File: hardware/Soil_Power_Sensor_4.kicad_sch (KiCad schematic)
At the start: 10 parts, among them J5 BOOT, J6 UART, U9 ESP32-C3-MINI-1-N4

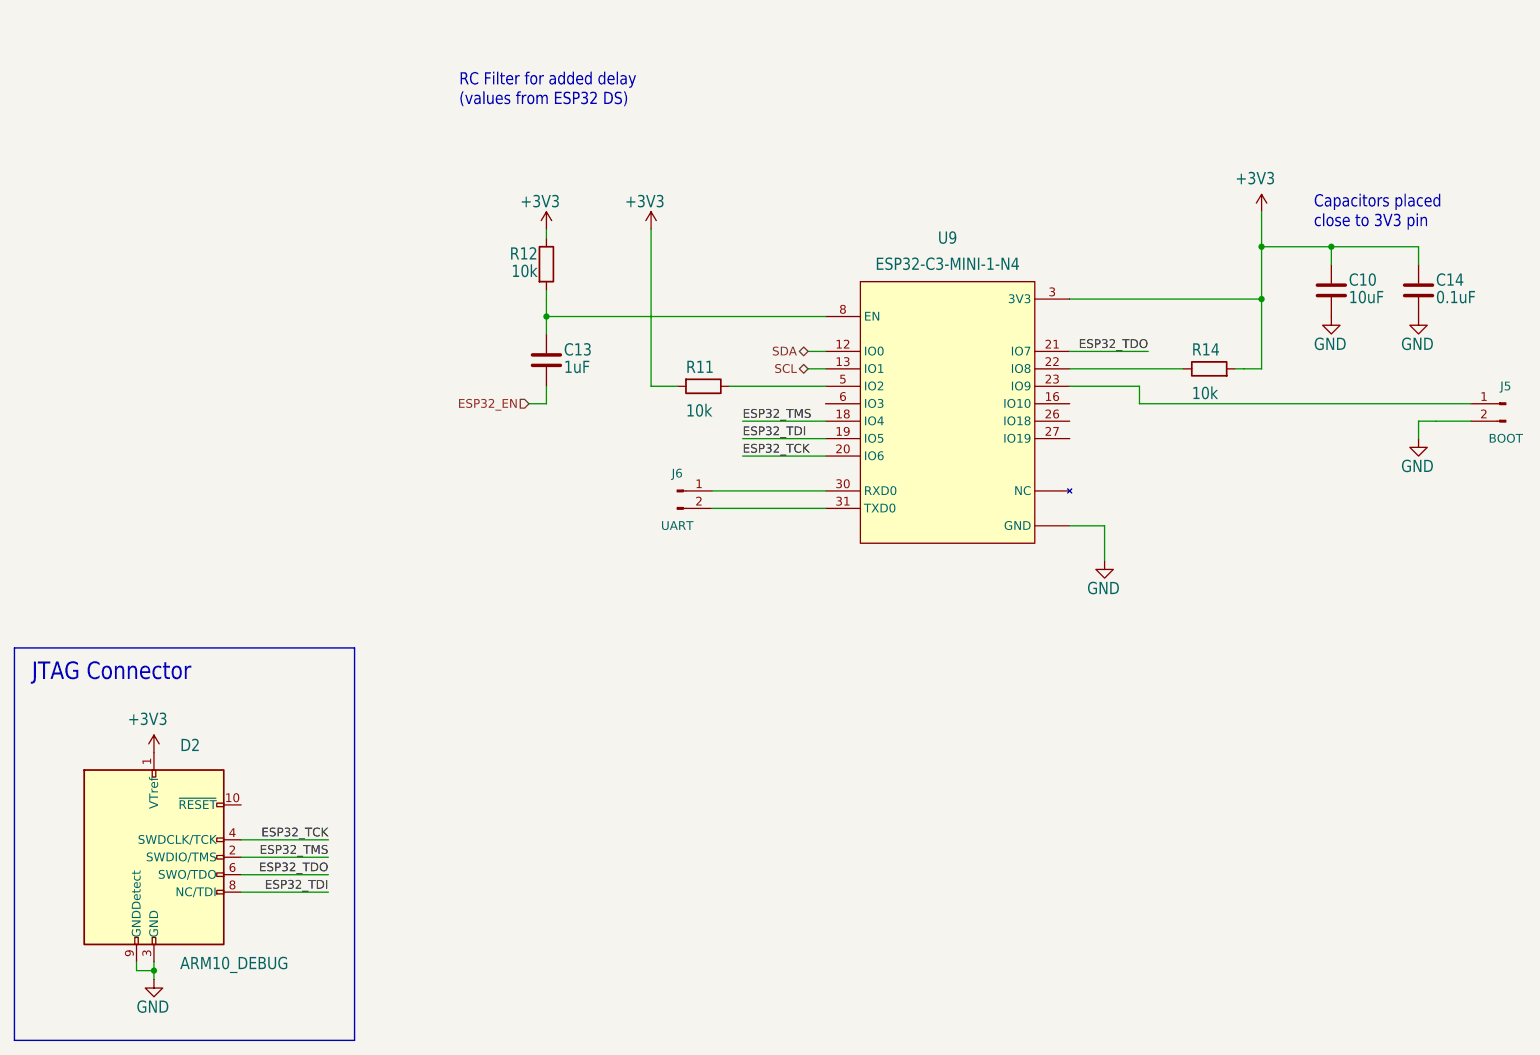
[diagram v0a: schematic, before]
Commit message: Adding general improvements to sensor PCB
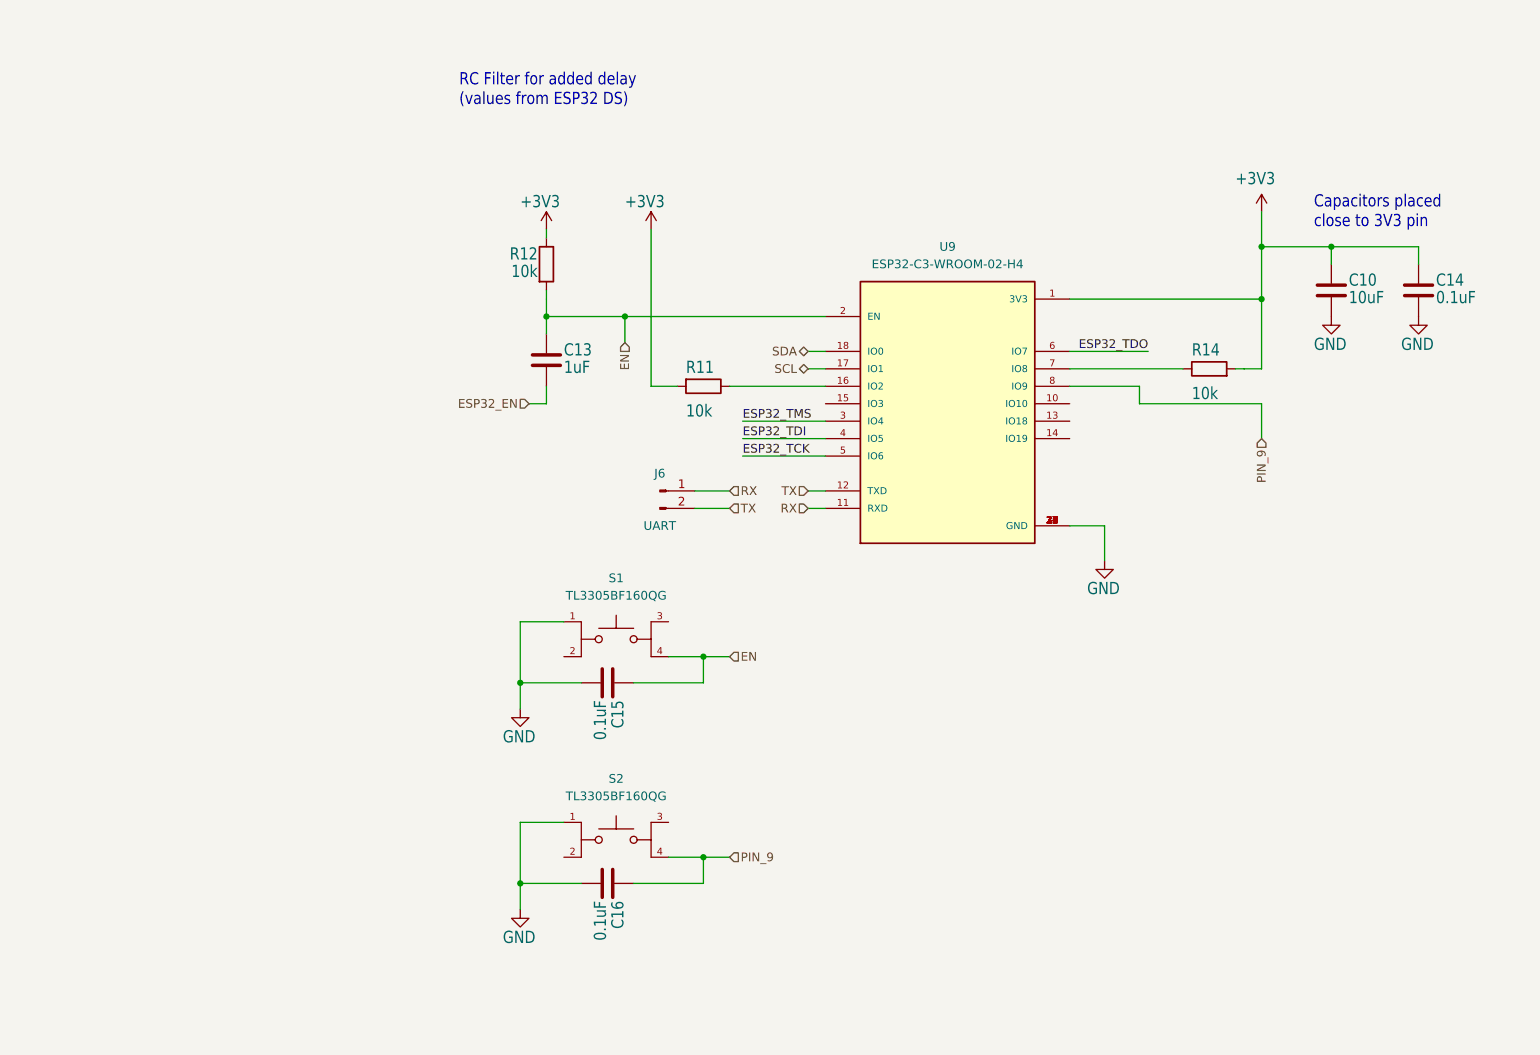
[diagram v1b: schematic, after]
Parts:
- removed D2: ARM10_DEBUG, Soil Power Sensor:ARM10_DEBUG, symbol Connector:Conn_ARM_JTAG_SWD_10
- removed J5: BOOT, Connector_PinHeader_2.54mm:PinHeader_1x02_P2.54mm_Vertical, symbol Connector:Conn_01x02_Pin
- removed U9: ESP32-C3-MINI-1-N4, Soil Power Sensor:XCVR_ESP32-C3-MINI-1-N4, symbol Soil Power Sensor-eagle-import:ESP32-C3-MINI-1-N4
- added C15, C16: 0.1uF, Capacitor_SMD:C_0603_1608Metric, symbol Device:C
- added S1, S2: TL3305BF160QG, TL3305BF160QG:SW_TL3305BF160QG, symbol TL3305BF160QG:TL3305BF160QG
- added U9: ESP32-C3-WROOM-02-H4, ESP32-C3-WROOM-02-H4:MODULE_ESP32-C3-WROOM-02-H4, symbol ESP32-C3-WROOM-02-H4:ESP32-C3-WROOM-02-H4
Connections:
- net +3V3: now also U9.1 (3V3)
- net ESP32_TCK: now also U9.5 (IO6)
- net ESP32_TDI: now also U9.4 (IO5)
- net ESP32_TDO: now also U9.6 (IO7)
- net ESP32_TMS: now also U9.3 (IO4)
- net GND: now also C15.2, C16.2, S1.1, S2.1, U9.19 (GND), U9.20 (GND), U9.21 (GND), U9.22 (GND), U9.23 (GND), U9.24 (GND), U9.25 (GND), U9.26 (GND), U9.27 (GND), U9.28 (GND), U9.29 (GND), U9.30 (GND), U9.31 (GND), U9.32 (GND), U9.33 (GND), U9.34 (GND), U9.35 (GND), U9.36 (GND), U9.37 (GND), U9.38 (GND), U9.39 (GND), U9.9 (GND)
- net SCL: now also U9.17 (IO1)
- net SDA: now also U9.18 (IO0)
- net at R11.1: now also U9.16 (IO2)
- net EN: now reaches C13.1, R12.2
- net EN: now also C15.1, S1.4, U9.2 (EN)
- net at R14.1: now also U9.7 (IO8)
- net RX: now reaches J6.1 (Pin_1)
- net RX: now also U9.11 (RXD)
- net TX: now reaches J6.2 (Pin_2)
- net TX: now also U9.12 (TXD)
- new net PIN_9: C16.1, S2.4, U9.8 (IO9)
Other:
- note removed: "JTAG Connector"
- moved on the sheet: J6

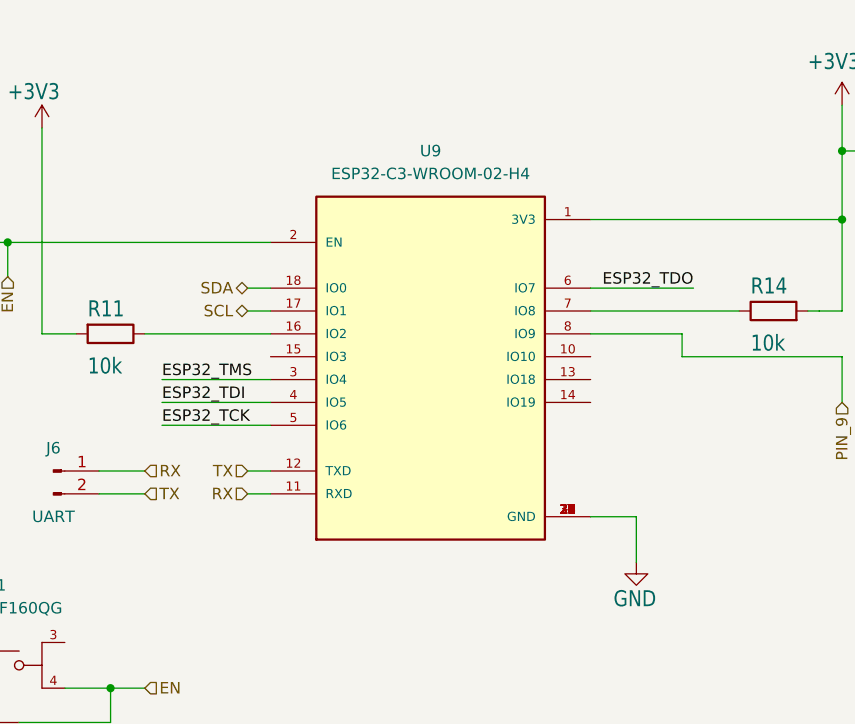
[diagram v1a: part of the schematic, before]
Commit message: Updated ESP32 module
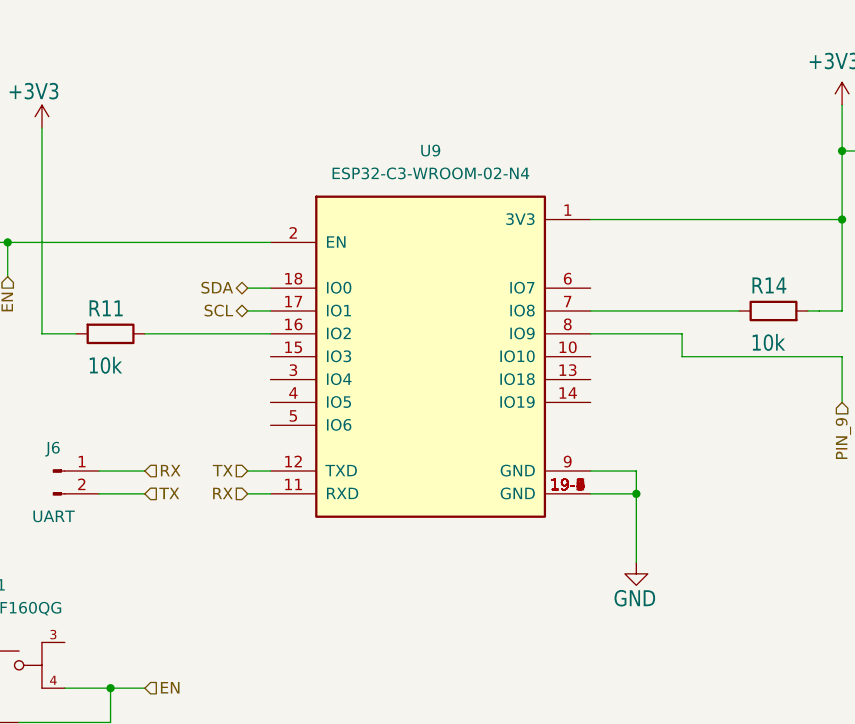
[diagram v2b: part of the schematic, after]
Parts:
- removed U9: ESP32-C3-WROOM-02-H4, ESP32-C3-WROOM-02-H4:MODULE_ESP32-C3-WROOM-02-H4, symbol ESP32-C3-WROOM-02-H4:ESP32-C3-WROOM-02-H4
- added U9: ESP32-C3-WROOM-02-N4, Soil Power Sensor:MODULE_ESP32-C3-WROOM-02-N4, symbol Soil Power Sensor-eagle-import:ESP32-C3-WROOM-02-N4
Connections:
- net +3V3: now also U9.1 (3V3)
- net EN: now also U9.2 (EN)
- net GND: now also U9.19-1 (GND), U9.19-2 (GND), U9.19-3 (GND), U9.19-4 (GND), U9.19-5 (GND), U9.19-6 (GND), U9.19-7 (GND), U9.19-8 (GND), U9.19-9 (GND), U9.9 (GND)
- net PIN_9: now also U9.8 (IO9)
- net RX: now also U9.11 (RXD)
- net SCL: now also U9.17 (IO1)
- net SDA: now also U9.18 (IO0)
- net TX: now also U9.12 (TXD)
- net at R11.1: now also U9.16 (IO2)
- net at R14.1: now also U9.7 (IO8)

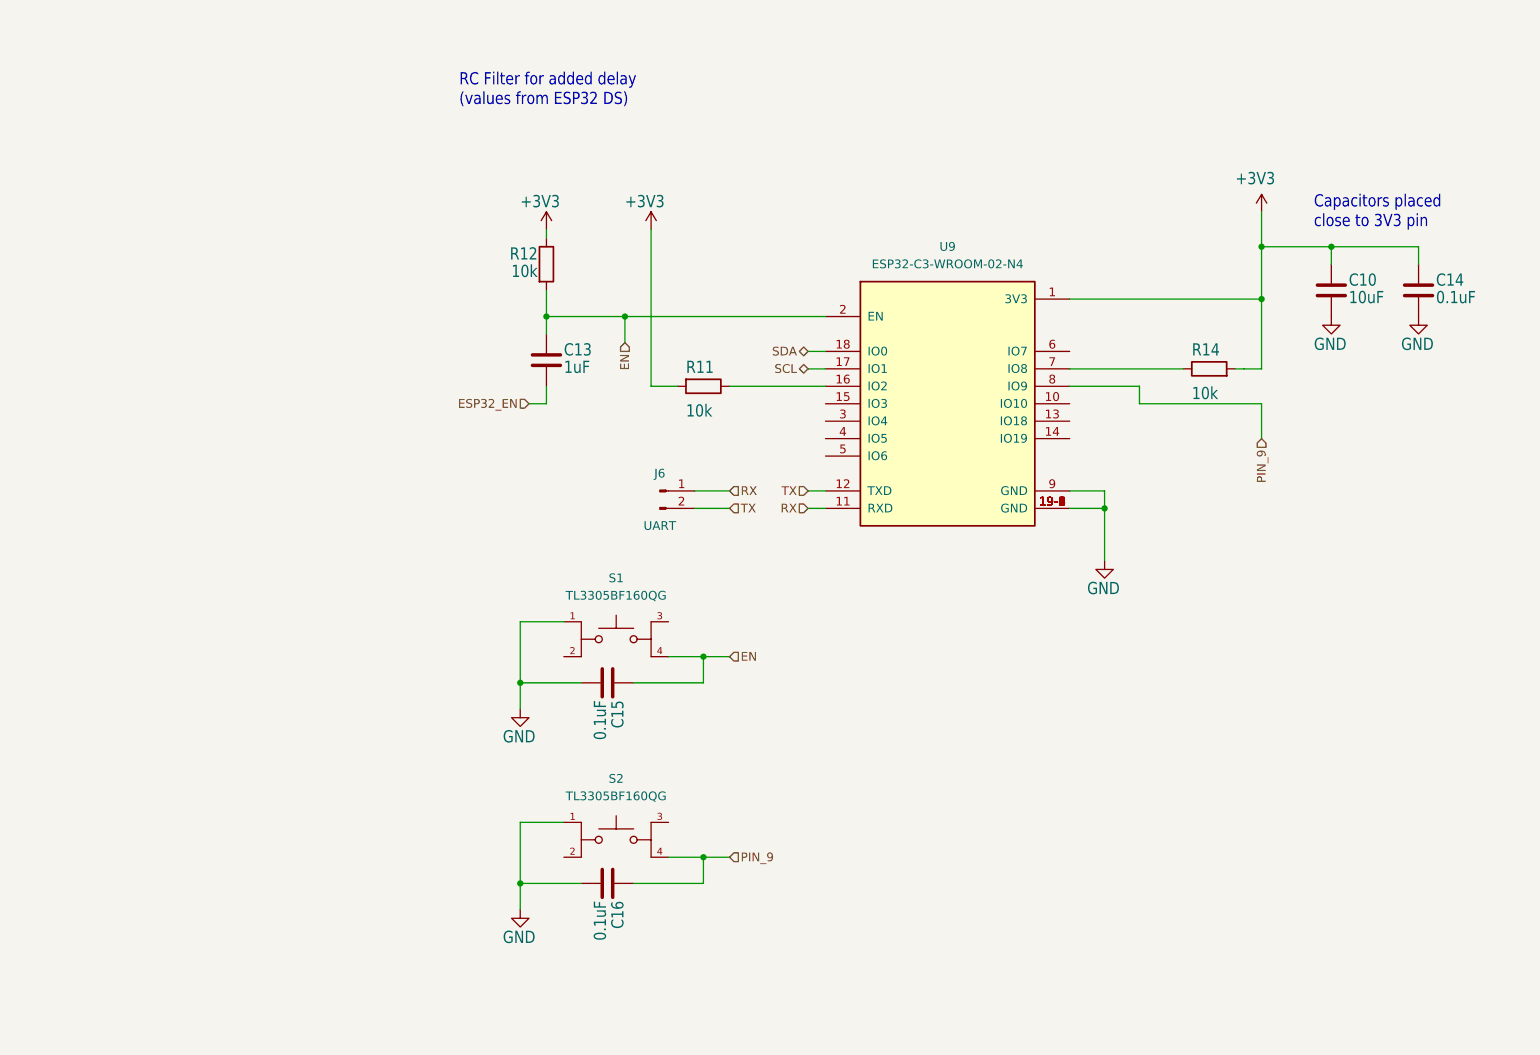
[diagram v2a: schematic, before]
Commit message: Added buttons for ESP32
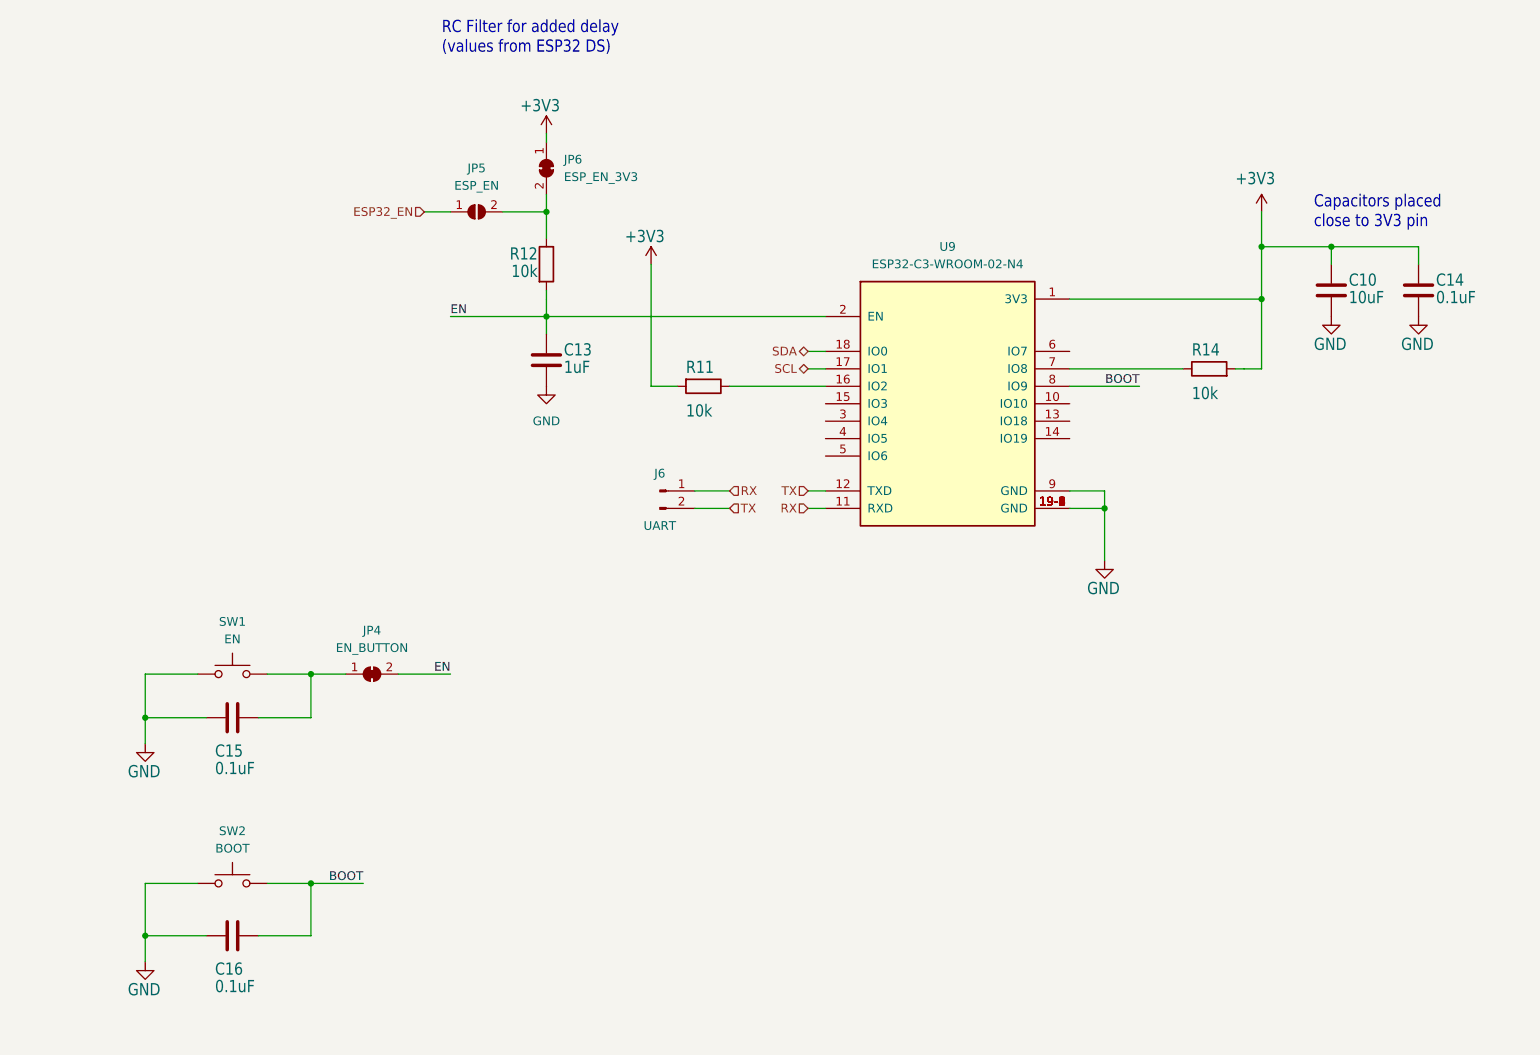
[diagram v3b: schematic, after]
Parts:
- removed S1, S2: TL3305BF160QG, TL3305BF160QG:SW_TL3305BF160QG, symbol TL3305BF160QG:TL3305BF160QG
- added JP4: EN_BUTTON, symbol Jumper:SolderJumper_2_Bridged
- added JP5: ESP_EN, symbol Jumper:SolderJumper_2_Open
- added JP6: ESP_EN_3V3, symbol Jumper:SolderJumper_2_Bridged
- added SW1: EN, Button_Switch_SMD:SW_Push_1P1T_NO_CK_KSC7xxJ, symbol Switch:SW_Push
- added SW2: BOOT, Button_Switch_SMD:SW_Push_1P1T_NO_CK_KSC7xxJ, symbol Switch:SW_Push
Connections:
- net +3V3: now also JP6.1 (A); no longer R12.1
- net EN: now also JP4.2 (B); no longer C15.1
- net ESP32_EN: now also JP5.1 (A); no longer C13.2
- net GND: now also C13.2, SW1.1, SW2.1
- net PIN_9 renamed BOOT
- net BOOT: now also SW2.2
- new net: JP5.2 (B), JP6.2 (B), R12.1
- new net: C15.1, JP4.1 (A), SW1.2
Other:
- moved on the sheet: C15, C16
